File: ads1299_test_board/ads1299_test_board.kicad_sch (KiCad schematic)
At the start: 0 parts

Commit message: PCB design charger and power supply
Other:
- sheet USB ports: added none; removed Vusb_charge
- sheet charger ports: added Vbat_out; removed Vusb_charge
- sheet power_circuit ports: added Vbat_out; removed none
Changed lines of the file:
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@@
 	(paper "A4")
 	(junction
-		(at 137.16 125.73)
+		(at 139.7 125.73)
 		(diameter 0)
 		(color 0 0 0 0)
@@
 	(wire
 		(pts
-			(xy 137.16 125.73) (xy 137.16 143.51)
+			(xy 139.7 125.73) (xy 139.7 143.51)
 		)
 		(stroke
@@
 	(wire
 		(pts
+			(xy 139.7 125.73) (xy 153.67 125.73)
+		)
+		(stroke
+			(width 0)
+			(type default)
+		)
+	)
+	(wire
+		(pts
 			(xy 137.16 118.11) (xy 137.16 102.87)
 		)
@@
 	(wire
 		(pts
-			(xy 138.43 147.32) (xy 134.62 147.32)
-		)
-		(stroke
-			(width 0)
-			(type default)
-		)
-	)
-	(wire
-		(pts
-			(xy 137.16 125.73) (xy 153.67 125.73)
-		)
-		(stroke
-			(width 0)
-			(type default)
-		)
-	)
-	(wire
-		(pts
-			(xy 134.62 125.73) (xy 137.16 125.73)
+			(xy 134.62 125.73) (xy 139.7 125.73)
 		)
 		(stroke
@@
 	(wire
 		(pts
-			(xy 134.62 143.51) (xy 137.16 143.51)
+			(xy 134.62 143.51) (xy 139.7 143.51)
 		)
 		(stroke
@@
 	(wire
 		(pts
-			(xy 138.43 128.27) (xy 138.43 147.32)
-		)
-		(stroke
-			(width 0)
-			(type default)
-		)
-	)
-	(wire
-		(pts
-			(xy 134.62 128.27) (xy 135.89 128.27)
+			(xy 134.62 128.27) (xy 138.43 128.27)
 		)
 		(stroke
@@
 	(wire
 		(pts
-			(xy 153.67 128.27) (xy 138.43 128.27)
-		)
-		(stroke
-			(width 0)
-			(type default)
-		)
-	)
-	(wire
-		(pts
 			(xy 134.62 69.85) (xy 153.67 69.85)
 		)
@@
 	(wire
 		(pts
+			(xy 137.16 138.43) (xy 137.16 130.81)
+		)
+		(stroke
+			(width 0)
+			(type default)
+		)
+	)
+	(wire
+		(pts
 			(xy 151.13 100.33) (xy 151.13 120.65)
 		)
@@
 	(wire
 		(pts
-			(xy 135.89 128.27) (xy 135.89 140.97)
+			(xy 138.43 128.27) (xy 138.43 140.97)
 		)
 		(stroke
@@
 	(wire
 		(pts
+			(xy 134.62 138.43) (xy 137.16 138.43)
+		)
+		(stroke
+			(width 0)
+			(type default)
+		)
+	)
+	(wire
+		(pts
 			(xy 134.62 62.23) (xy 153.67 62.23)
 		)
@@
 	(wire
 		(pts
-			(xy 135.89 140.97) (xy 134.62 140.97)
+			(xy 138.43 140.97) (xy 134.62 140.97)
+		)
+		(stroke
+			(width 0)
+			(type default)
+		)
+	)
+	(wire
+		(pts
+			(xy 134.62 130.81) (xy 137.16 130.81)
 		)
 		(stroke
@@
 			)
 		)
-		(pin "Vusb_charge" input
-			(at 134.62 147.32 0)
+		(pin "Vbat_out" output
+			(at 134.62 138.43 0)
 			(effects
 				(font
@@
 			)
 		)
-		(pin "Vusb_charge" output
-			(at 153.67 128.27 180)
-			(effects
-				(font
-					(size 1.27 1.27)
-				)
-				(justify left)
-			)
-		)
 		(instances
 			(project "ads1299_test_board"
@@
 			(effects
 				(font
+					(size 1.27 1.27)
+				)
+				(justify right)
+			)
+		)
+		(pin "Vbat_out" input
+			(at 134.62 130.81 0)
+			(effects
+				(font

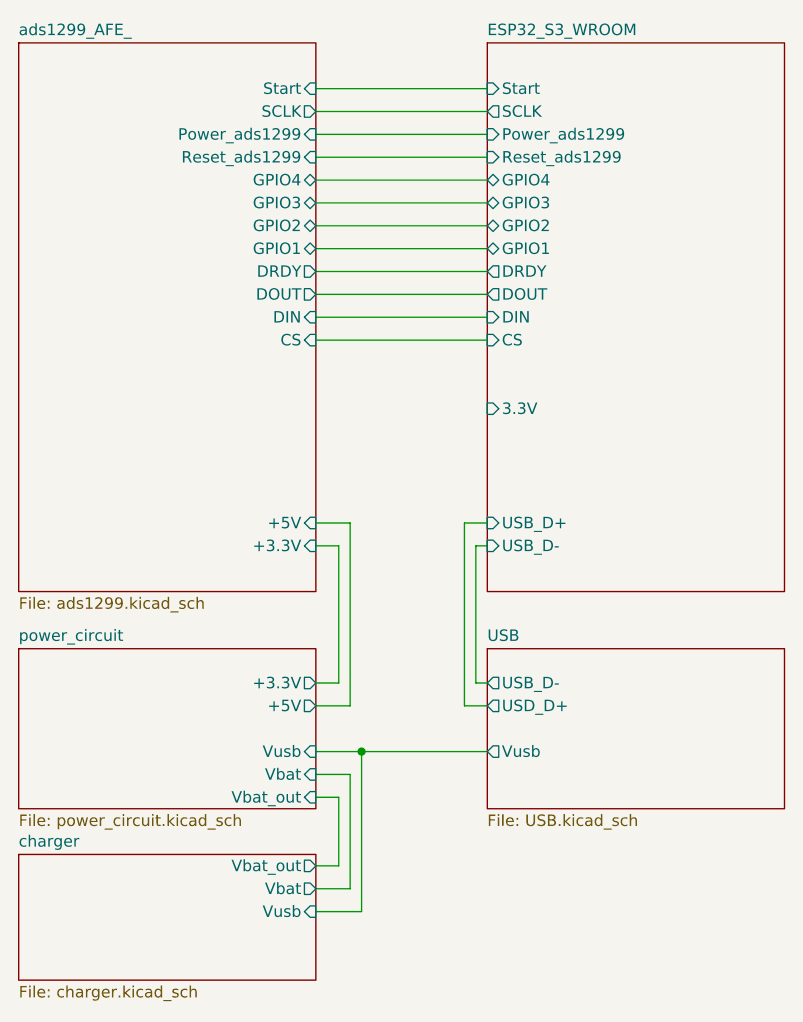
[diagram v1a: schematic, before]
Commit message: top layer almost finished, bottom layer preview
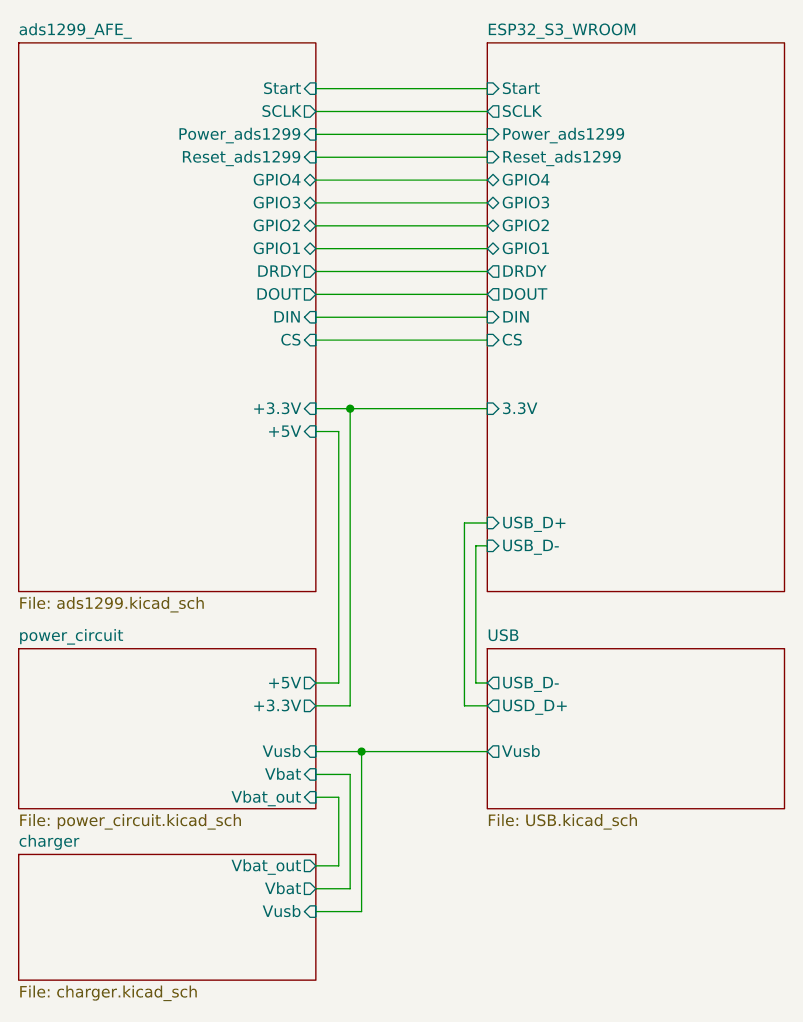
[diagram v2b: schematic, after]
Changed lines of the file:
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@@
 	(paper "A4")
+	(junction
+		(at 138.43 87.63)
+		(diameter 0)
+		(color 0 0 0 0)
+	)
 	(junction
 		(at 139.7 125.73)
@@
 	(wire
 		(pts
-			(xy 138.43 100.33) (xy 138.43 120.65)
+			(xy 137.16 90.17) (xy 137.16 118.11)
 		)
 		(stroke
@@
 	(wire
 		(pts
-			(xy 137.16 118.11) (xy 137.16 102.87)
-		)
-		(stroke
-			(width 0)
-			(type default)
-		)
-	)
-	(wire
-		(pts
 			(xy 134.62 125.73) (xy 139.7 125.73)
 		)
@@
 	(wire
 		(pts
-			(xy 137.16 102.87) (xy 134.62 102.87)
+			(xy 134.62 87.63) (xy 138.43 87.63)
 		)
 		(stroke
@@
 	(wire
 		(pts
-			(xy 138.43 120.65) (xy 134.62 120.65)
+			(xy 137.16 118.11) (xy 134.62 118.11)
 		)
 		(stroke
@@
 	(wire
 		(pts
+			(xy 138.43 87.63) (xy 138.43 120.65)
+		)
+		(stroke
+			(width 0)
+			(type default)
+		)
+	)
+	(wire
+		(pts
 			(xy 151.13 100.33) (xy 151.13 120.65)
 		)
@@
 	(wire
 		(pts
+			(xy 153.67 87.63) (xy 138.43 87.63)
+		)
+		(stroke
+			(width 0)
+			(type default)
+		)
+	)
+	(wire
+		(pts
 			(xy 153.67 118.11) (xy 152.4 118.11)
 		)
@@
 	(wire
 		(pts
-			(xy 134.62 118.11) (xy 137.16 118.11)
+			(xy 134.62 120.65) (xy 138.43 120.65)
 		)
 		(stroke
@@
 	(wire
 		(pts
-			(xy 134.62 100.33) (xy 138.43 100.33)
+			(xy 134.62 90.17) (xy 137.16 90.17)
 		)
 		(stroke
@@
 		)
 		(pin "+3.3V" output
+			(at 134.62 120.65 0)
+			(effects
+				(font
+					(size 1.27 1.27)
+				)
+				(justify right)
+			)
+		)
+		(pin "+5V" output
 			(at 134.62 118.11 0)
-			(effects
-				(font
-					(size 1.27 1.27)
-				)
-				(justify right)
-			)
-		)
-		(pin "+5V" output
-			(at 134.62 120.65 0)
 			(effects
 				(font
@@
 		)
 		(pin "+3.3V" input
-			(at 134.62 102.87 0)
+			(at 134.62 87.63 0)
 			(effects
 				(font
@@
 		)
 		(pin "+5V" input
-			(at 134.62 100.33 0)
-			(effects
-				(font
+			(at 134.62 90.17 0)
+			(effects
+				(font
